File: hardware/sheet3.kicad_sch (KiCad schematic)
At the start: 23 parts, among them J1 DC-005-5A-2.0, U1 AP63205WU-7, U3 AP2114H-3.3TRG1

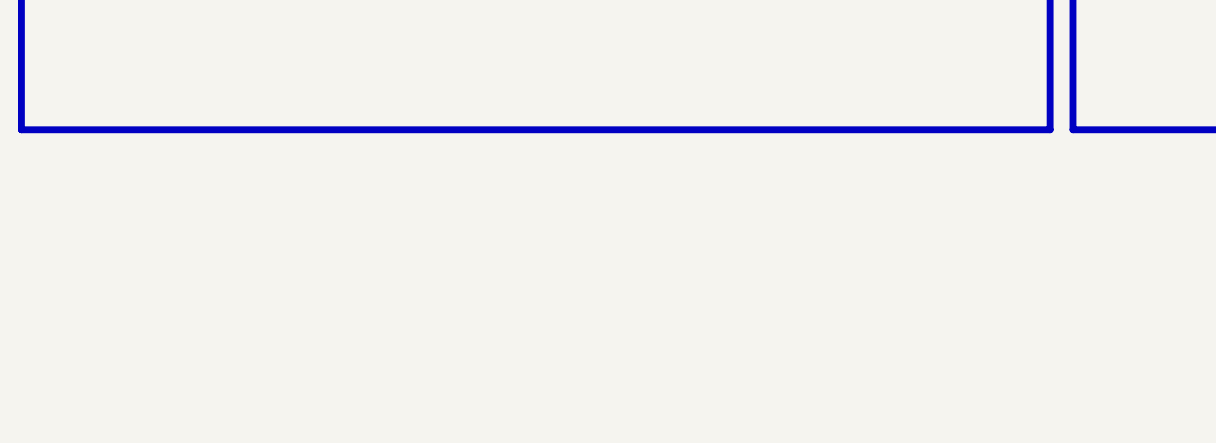
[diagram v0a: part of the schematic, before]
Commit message: hardware(feat): add mounting holes and fiducials
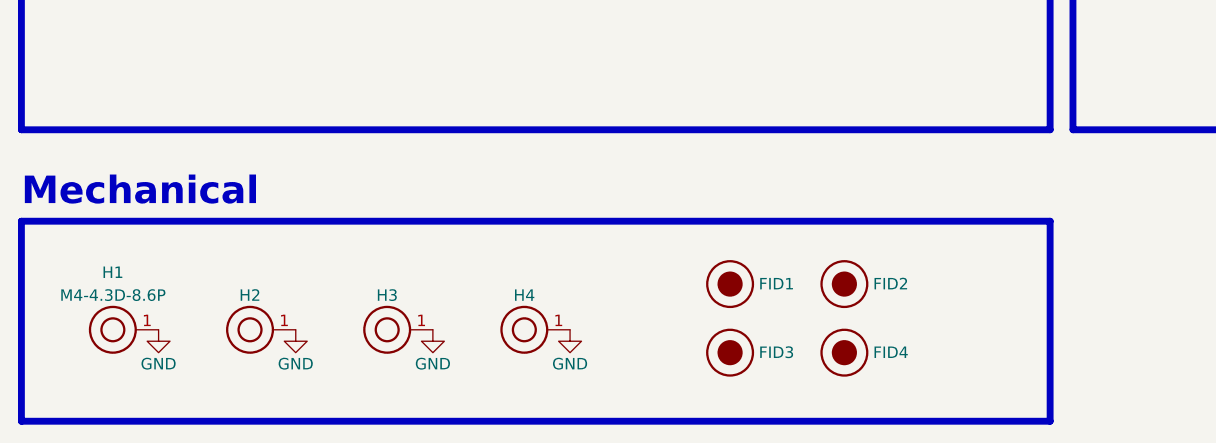
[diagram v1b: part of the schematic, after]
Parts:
- added FID1, FID2, FID3, FID4: 1.0P-2.0M, 12_mechanical:Fiducial_1mm_Mask2mm, symbol 12_mechanical:FID_1.0P-2.0M
- added H1, H2, H3, H4: M4-4.3D-8.6P, 12_mechanical:MountingHole_4.3mm_M4_Pad, symbol 12_mechanical:MH_M4-4.3D-8.6P
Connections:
- net GND: now also H1.1, H2.1, H3.1, H4.1
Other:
- note added: "Mechanical"
